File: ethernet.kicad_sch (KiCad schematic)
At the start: 40 parts, among them J1001 7499010121A, U1001 LAN8742A-CZ-TR, U1002 USBLC6-4SC6

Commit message: Clean up schematics
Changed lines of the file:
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@@
 	(title_block
 		(title "Linux SBC")
-		(date "2025-12-19")
+		(date "2025-12-26")
 		(rev "v1.0.0")
 	)
@@
 	(text_box "Route as 50 Ω single-ended.\n\nEnsure that the skew between ETH.[T|R]XD0 and ETH.[T|R]XD1 is minimized."
 		(exclude_from_sim no)
-		(at 44.45 152.4 0)
+		(at 76.2 209.55 0)
 		(size 34.29 12.7)
 		(margins 0.9525 0.9525 0.9525 0.9525)
@@
 		(polyline
 			(pts
-				(xy 190.5 168.91) (xy 193.04 168.91) (xy 193.04 204.47) (xy 190.5 204.47)
+				(xy 190.5 204.47) (xy 193.04 204.47) (xy 193.04 168.91) (xy 190.5 168.91)
 			)
 			(stroke
@@
 		(polyline
 			(pts
-				(xy 73.66 168.91) (xy 76.2 168.91) (xy 76.2 204.47) (xy 73.66 204.47)
+				(xy 76.2 204.47) (xy 73.66 204.47) (xy 73.66 168.91) (xy 76.2 168.91)
 			)
 			(stroke
@@
 		(length 2.54)
 		(shape round)
-		(at 191.77 168.91 0)
+		(at 191.77 204.47 180)
 		(fields_autoplaced yes)
 		(effects
@@
 				(size 1.27 1.27)
 			)
-			(justify left bottom)
+			(justify right bottom)
 		)
 		(property "Netclass" "ETH"
-			(at 192.4685 166.37 0)
+			(at 191.0715 207.01 0)
 			(effects
 				(font
 					(size 1.27 1.27)
 				)
-				(justify left)
+				(justify right)
 			)
 		)
 		(property "Component Class" ""
-			(at 36.83 20.32 0)
+			(at 346.71 55.88 0)
 			(effects
 				(font
@@
 					(italic yes)
 				)
-				(justify right)
+				(justify left)
 			)
 		)
@@
 		(length 2.54)
 		(shape round)
-		(at 74.93 168.91 0)
+		(at 74.93 204.47 180)
 		(fields_autoplaced yes)
 		(effects
@@
 				(size 1.27 1.27)
 			)
-			(justify left bottom)
+			(justify right bottom)
 		)
 		(property "Netclass" "ETH"
-			(at 75.6285 166.37 0)
+			(at 75.6285 207.01 0)
 			(effects
 				(font
@@
 		)
 		(property "Component Class" ""
-			(at -80.01 20.32 0)
+			(at -80.01 55.88 0)
 			(effects
 				(font

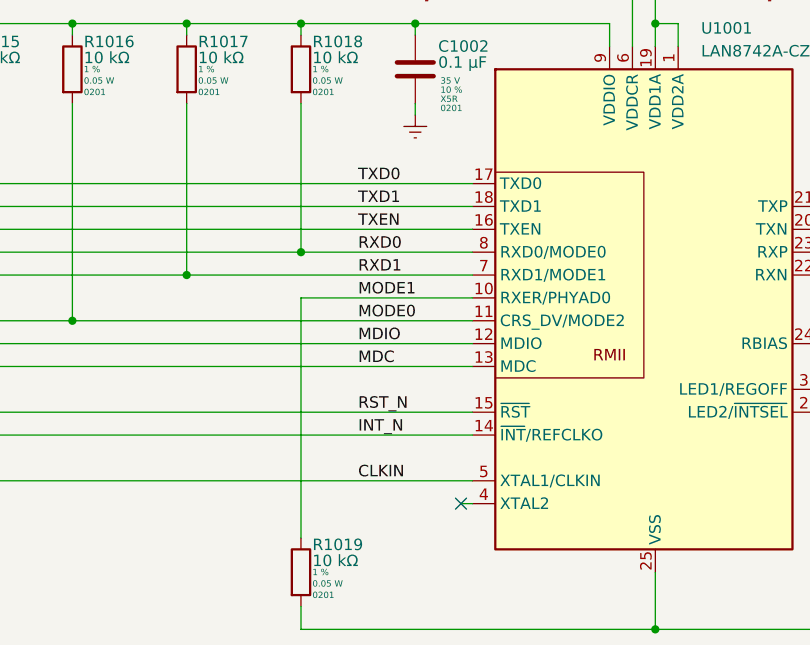
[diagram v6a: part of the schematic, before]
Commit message: Ethernet: Fix net names
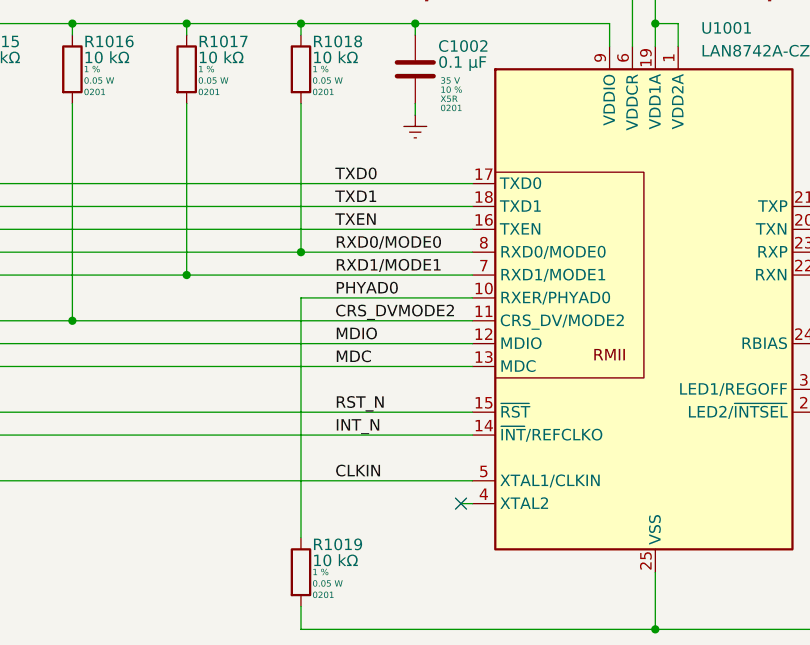
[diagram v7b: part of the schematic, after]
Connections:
- net MODE0 renamed CRS_DVMODE2
- net MODE1 renamed PHYAD0
- net RXD0 renamed RXD0/MODE0
- net RXD1 renamed RXD1/MODE1
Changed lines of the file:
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@@
 	)
 	(label "TXD0"
-		(at 182.88 170.18 0)
+		(at 180.34 170.18 0)
 		(effects
 			(font
@@
 	)
 	(label "MDC"
-		(at 182.88 190.5 0)
+		(at 180.34 190.5 0)
 		(effects
 			(font
@@
 		)
 	)
-	(label "RXD1"
-		(at 182.88 180.34 0)
+	(label "RXD1{slash}MODE1"
+		(at 180.34 180.34 0)
 		(effects
 			(font
@@
 	)
 	(label "TXD1"
-		(at 182.88 172.72 0)
+		(at 180.34 172.72 0)
 		(effects
 			(font
@@
 	)
 	(label "RST_N"
-		(at 182.88 195.58 0)
+		(at 180.34 195.58 0)
 		(effects
 			(font
@@
 	)
 	(label "TXEN"
-		(at 182.88 175.26 0)
+		(at 180.34 175.26 0)
 		(effects
 			(font
@@
 		)
 	)
-	(label "MODE0"
-		(at 182.88 185.42 0)
+	(label "CRS_DVMODE2"
+		(at 180.34 185.42 0)
 		(effects
 			(font
@@
 	)
 	(label "MDIO"
-		(at 182.88 187.96 0)
-		(effects
-			(font
-				(size 1.27 1.27)
-			)
-			(justify left bottom)
-		)
-	)
-	(label "RXD0"
-		(at 182.88 177.8 0)
+		(at 180.34 187.96 0)
+		(effects
+			(font
+				(size 1.27 1.27)
+			)
+			(justify left bottom)
+		)
+	)
+	(label "RXD0{slash}MODE0"
+		(at 180.34 177.8 0)
 		(effects
 			(font
@@
 	)
 	(label "CLKIN"
-		(at 182.88 203.2 0)
+		(at 180.34 203.2 0)
 		(effects
 			(font
@@
 		)
 	)
-	(label "MODE1"
-		(at 182.88 182.88 0)
+	(label "PHYAD0"
+		(at 180.34 182.88 0)
 		(effects
 			(font
@@
 	)
 	(label "INT_N"
-		(at 182.88 198.12 0)
+		(at 180.34 198.12 0)
 		(effects
 			(font
@@
 		(polyline
 			(pts
-				(xy 190.5 204.47) (xy 193.04 204.47) (xy 193.04 168.91) (xy 190.5 168.91)
+				(xy 172.72 204.47) (xy 177.8 204.47) (xy 177.8 168.91) (xy 172.72 168.91)
 			)
 			(stroke
@@
 		(length 2.54)
 		(shape round)
-		(at 191.77 204.47 180)
+		(at 173.99 204.47 180)
 		(fields_autoplaced yes)
 		(effects
@@
 		)
 		(property "Netclass" "ETH"
-			(at 191.0715 207.01 0)
+			(at 173.2915 207.01 0)
 			(effects
 				(font
@@
 		)
 		(property "Component Class" ""
-			(at 346.71 55.88 0)
+			(at 328.93 55.88 0)
 			(effects
 				(font

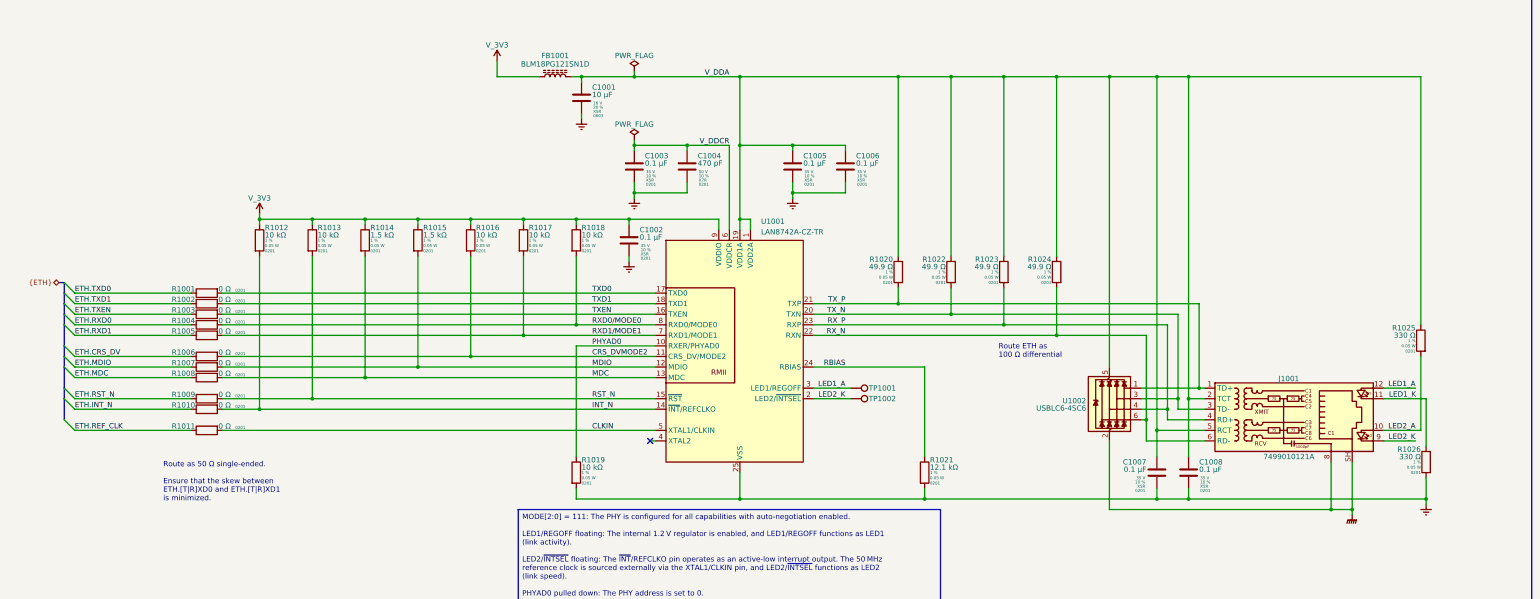
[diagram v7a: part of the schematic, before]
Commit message: ETH: Change TVS diode
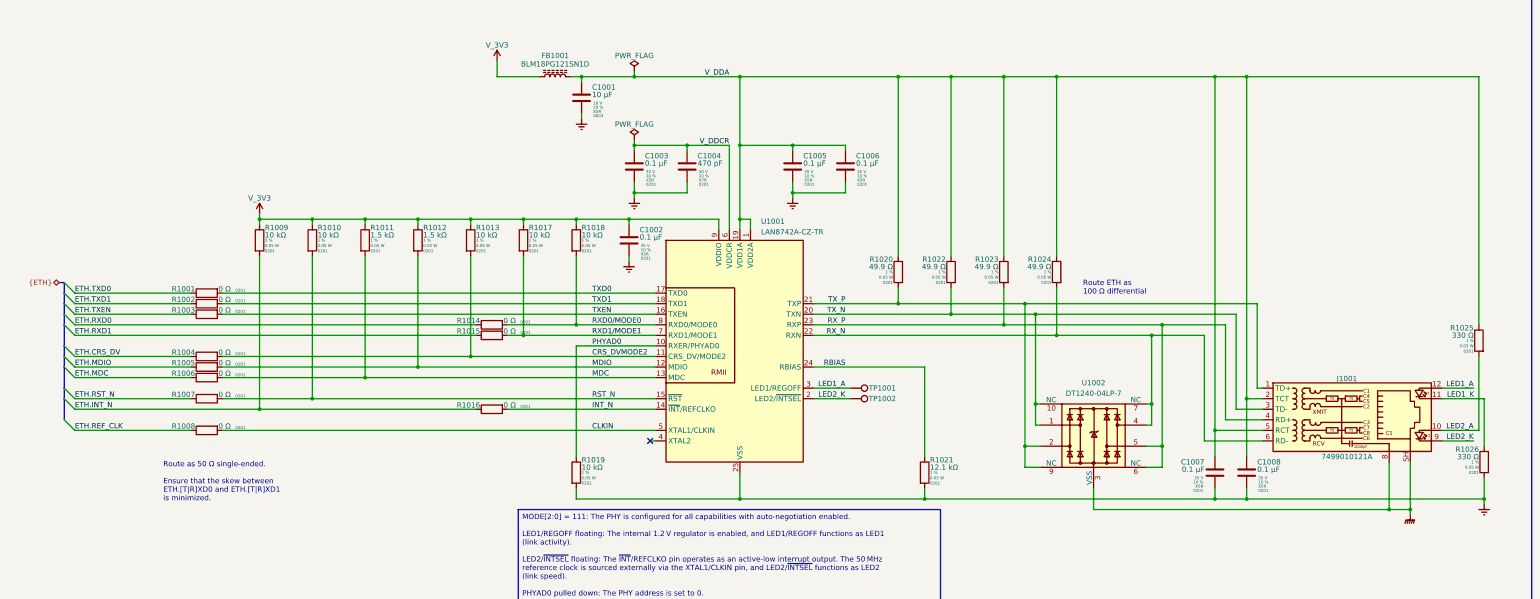
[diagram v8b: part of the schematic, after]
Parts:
- removed U1002: USBLC6-4SC6, Package_TO_SOT_SMD:SOT-23-6, symbol Power_Protection:USBLC6-4SC6
- added U1002: DT1240-04LP-7, Package_DFN_QFN:Diodes_UDFN-10_1.0x2.5mm_P0.5mm, symbol Power_Protection:D3V3XA4B10LP
- renumbered R1006 to R1004, R1007 to R1005, R1008 to R1006, R1009 to R1007, R1011 to R1008, R1012 to R1009, R1013 to R1010, R1014 to R1011, R1015 to R1012, R1016 to R1013, R1004 to R1014, R1005 to R1015, R1010 to R1016
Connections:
- net CHASSIS: now also U1002.3 (VSS), U1002.8 (VSS)
- net ETH.INT_N: now also R1009.2
- net INT_N: no longer R1009.2
- net RX_N: now also U1002.4, U1002.7 (NC)
- net RX_P: now also U1002.5, U1002.6 (NC)
- net TX_N: now also U1002.1, U1002.10 (NC)
- net TX_P: now also U1002.2, U1002.9 (NC)
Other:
- moved on the sheet: C1007, C1008, J1001, R1014, R1015, R1016, R1025, R1026
